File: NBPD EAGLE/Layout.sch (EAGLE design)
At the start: 56 parts, among them IC1 4040N, IC2 4040N, IC3 4017N, IC4 4017N, IC5 4017N, IC6 4017N, IC7 7818TV, U1 LM317K, Y1 ACHL-32.768MHZ-EK

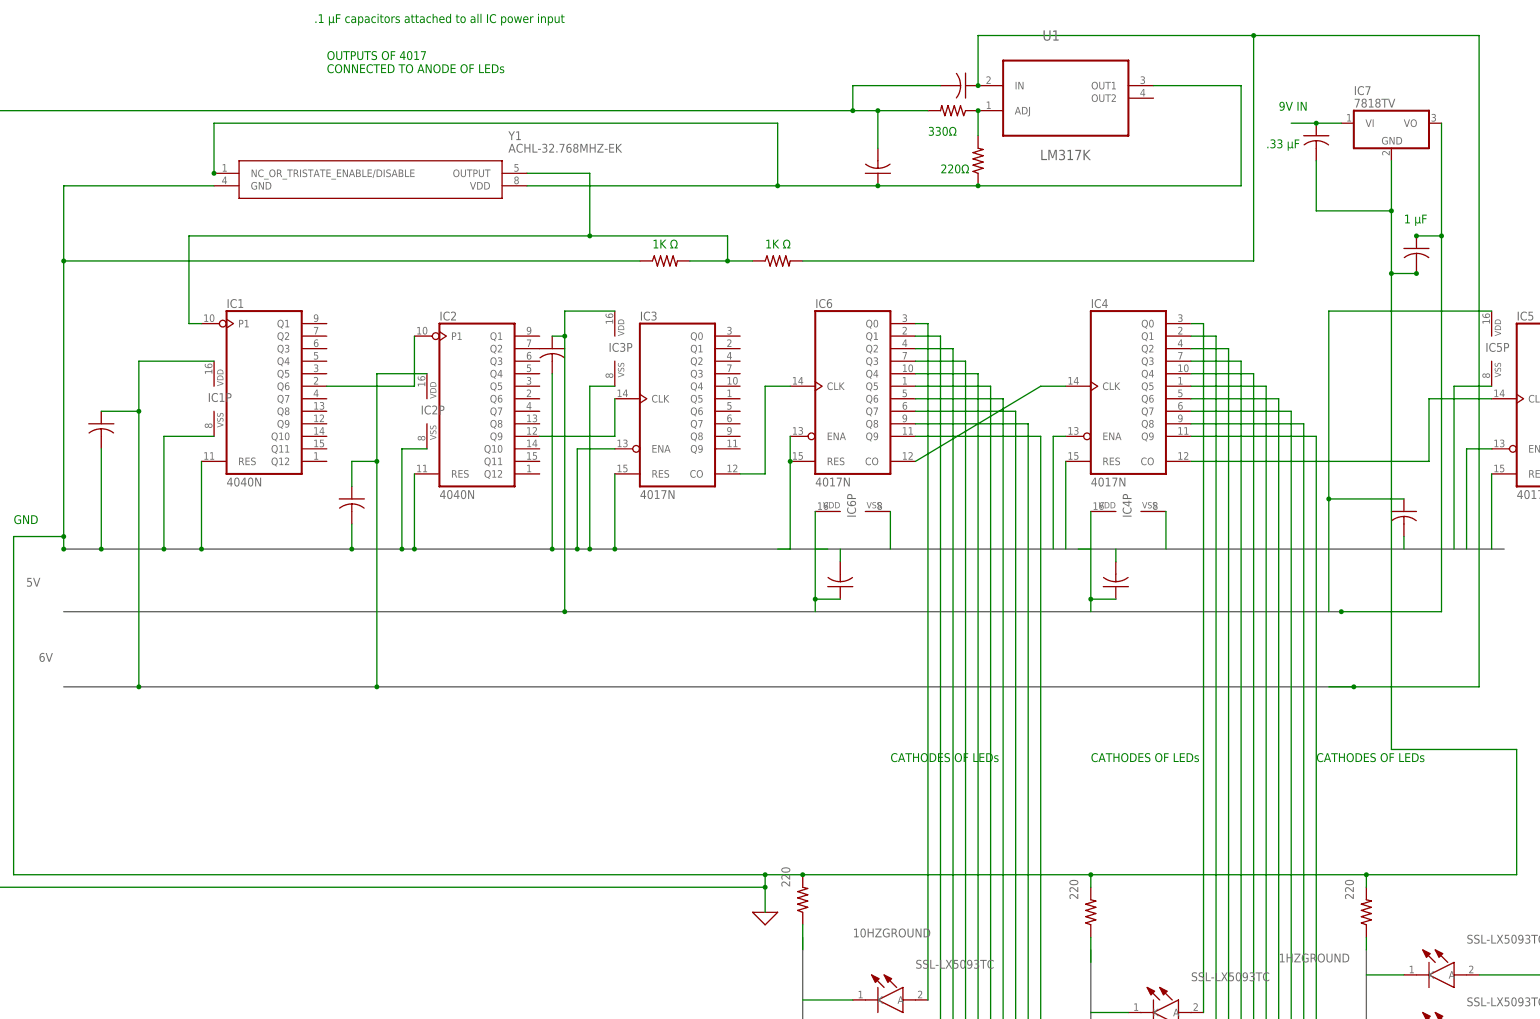
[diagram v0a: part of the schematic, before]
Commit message: Schematic Labels & PDF Names
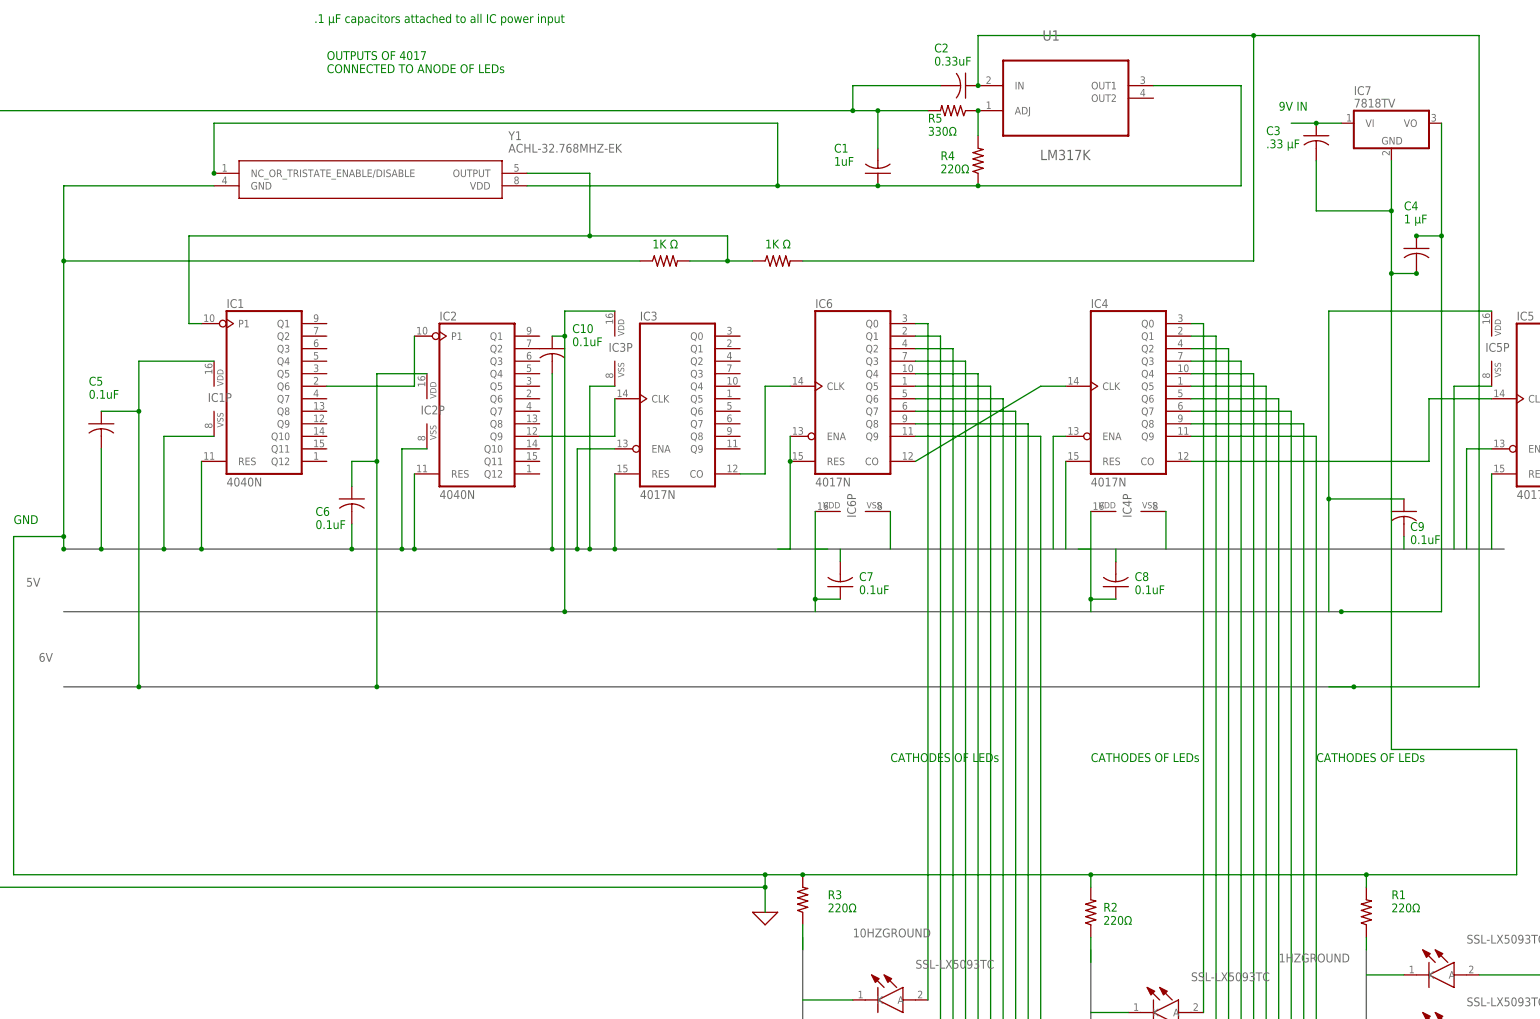
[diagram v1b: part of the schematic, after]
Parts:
- C3: value .1uF -> 0.33uF
- C5: C5 (none) -> 0.1uF; SPICEPREFIX (none) -> C
- IC7: SPICEPREFIX (none) -> J
- R1: R6 220 -> (none)
- R2: R5 220 -> (none)
- R3: R4 220 -> (none)
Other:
- note added: "C1 1uF"
- note added: "C10 0.1uF"
- note added: "C2 0.33uF"
- note added: "C3 .33 µF"
- note added: "C4 1 µF"
- note added: "C5 0.1uF"
- note added: "C6 0.1uF"
- note added: "C7 0.1uF"
- note added: "C8 0.1uF"
- note added: "C9 0.1uF"
- note added: "R1 220Ω"
- note added: "R2 220Ω"
- note added: "R3 220Ω"
- note added: "R4 220Ω"
- note added: "R5 330Ω"
- note removed: ".33 µF"
- note removed: "1 µF"
- note removed: "220Ω"
- note removed: "330Ω"

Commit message: Update PDF
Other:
- note added: "LED01"
- note added: "LED10"
- note added: "LED11"
- note added: "LED20"
- note added: "LED21"
- note added: "LED30"
- note added: "R6 1K Ω"
- note added: "R7 1K Ω"
- note added: "USE SN74HC4040 NOT CD74HC4040"
- note removed: "1K Ω"
- note removed: "OUTPUTS OF 4017 CONNECTED TO ANODE OF LEDs"

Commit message: 3.3V Update
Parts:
- removed R4: 220, rcl:R-US_0309/12
- removed R5: 330, rcl:R-US_0309/12
- removed U1: LM317K, LM317K:LM317K
- added IC8: 786TV, linear:786TV
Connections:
- removed net ADJ: R4.2, R5.1, U1.ADJ
- net 3.3: now also IC8.VO; no longer R4.1, U1.OUT1
- net 6V: now also IC8.VI; no longer U1.IN
- net N$1: now also IC8.GND; no longer R5.2
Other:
- note added: "C1 10uF"
- note added: "C2 100nF"
- note removed: "C1 1uF"
- note removed: "C2 0.33uF"
- note removed: "R4 220Ω"
- note removed: "R5 330Ω"
